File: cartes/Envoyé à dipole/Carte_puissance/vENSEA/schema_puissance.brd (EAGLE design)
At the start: 73.7 x 46.6 mm, 23 parts, among them X2 GMSTBA2

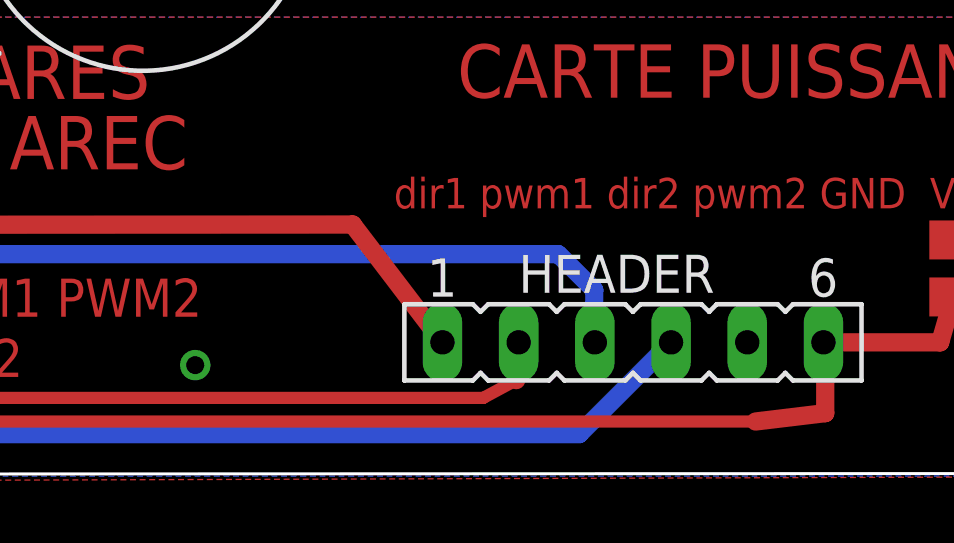
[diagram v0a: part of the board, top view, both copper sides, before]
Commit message: Maj carte puissance vENSEA + correction bug + modif carte RF-CAN
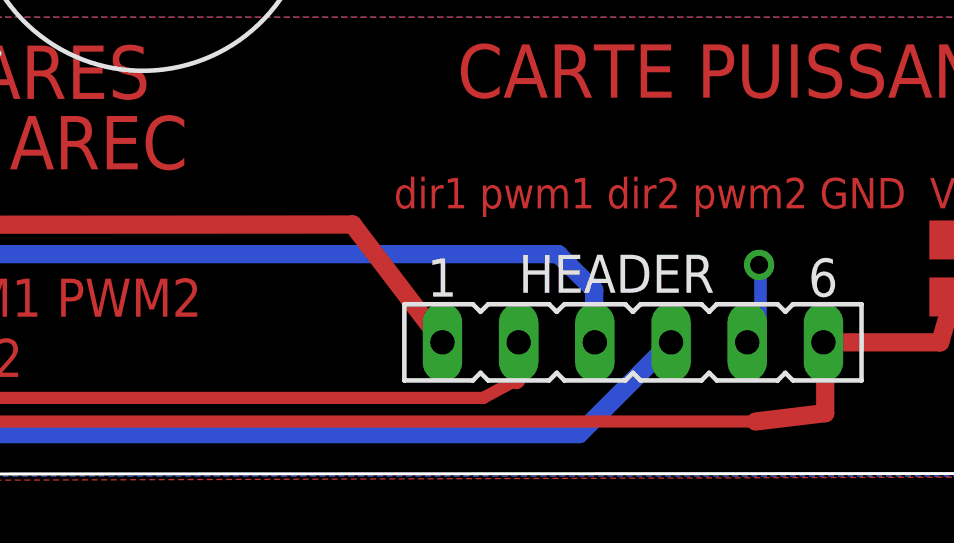
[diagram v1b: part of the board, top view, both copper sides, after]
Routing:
- net GND: track 1.31 -> 4.59 mm
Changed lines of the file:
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@@
 <layers>
 <layer number="1" name="Top" color="4" fill="1" visible="yes" active="yes"/>
-<layer number="16" name="Bottom" color="1" fill="1" visible="no" active="yes"/>
+<layer number="16" name="Bottom" color="1" fill="1" visible="yes" active="yes"/>
 <layer number="17" name="Pads" color="2" fill="1" visible="yes" active="yes"/>
 <layer number="18" name="Vias" color="2" fill="1" visible="yes" active="yes"/>
 <layer number="19" name="Unrouted" color="6" fill="1" visible="yes" active="yes"/>
-<layer number="20" name="Dimension" color="15" fill="1" visible="no" active="yes"/>
-<layer number="21" name="tPlace" color="7" fill="1" visible="no" active="yes"/>
-<layer number="22" name="bPlace" color="7" fill="1" visible="no" active="yes"/>
-<layer number="23" name="tOrigins" color="15" fill="1" visible="no" active="yes"/>
-<layer number="24" name="bOrigins" color="15" fill="1" visible="no" active="yes"/>
-<layer number="25" name="tNames" color="7" fill="1" visible="no" active="yes"/>
-<layer number="26" name="bNames" color="7" fill="1" visible="no" active="yes"/>
-<layer number="27" name="tValues" color="7" fill="1" visible="no" active="yes"/>
-<layer number="28" name="bValues" color="7" fill="1" visible="no" active="yes"/>
-<layer number="29" name="tStop" color="7" fill="3" visible="no" active="yes"/>
-<layer number="30" name="bStop" color="7" fill="6" visible="no" active="yes"/>
-<layer number="31" name="tCream" color="7" fill="4" visible="no" active="yes"/>
-<layer number="32" name="bCream" color="7" fill="5" visible="no" active="yes"/>
-<layer number="33" name="tFinish" color="6" fill="3" visible="no" active="yes"/>
-<layer number="34" name="bFinish" color="6" fill="6" visible="no" active="yes"/>
-<layer number="35" name="tGlue" color="7" fill="4" visible="no" active="yes"/>
-<layer number="36" name="bGlue" color="7" fill="5" visible="no" active="yes"/>
-<layer number="37" name="tTest" color="7" fill="1" visible="no" active="yes"/>
-<layer number="38" name="bTest" color="7" fill="1" visible="no" active="yes"/>
-<layer number="39" name="tKeepout" color="4" fill="11" visible="no" active="yes"/>
-<layer number="40" name="bKeepout" color="1" fill="11" visible="no" active="yes"/>
-<layer number="41" name="tRestrict" color="4" fill="10" visible="no" active="yes"/>
-<layer number="42" name="bRestrict" color="1" fill="10" visible="no" active="yes"/>
-<layer number="43" name="vRestrict" color="2" fill="10" visible="no" active="yes"/>
-<layer number="44" name="Drills" color="7" fill="1" visible="no" active="yes"/>
-<layer number="45" name="Holes" color="7" fill="1" visible="no" active="yes"/>
-<layer number="46" name="Milling" color="3" fill="1" visible="no" active="yes"/>
-<layer number="47" name="Measures" color="7" fill="1" visible="no" active="yes"/>
-<layer number="48" name="Document" color="7" fill="1" visible="no" active="yes"/>
-<layer number="49" name="Reference" color="7" fill="1" visible="no" active="yes"/>
-<layer number="50" name="dxf" color="7" fill="1" visible="no" active="yes"/>
-<layer number="51" name="tDocu" color="7" fill="1" visible="no" active="yes"/>
-<layer number="52" name="bDocu" color="7" fill="1" visible="no" active="yes"/>
+<layer number="20" name="Dimension" color="15" fill="1" visible="yes" active="yes"/>
+<layer number="21" name="tPlace" color="7" fill="1" visible="yes" active="yes"/>
+<layer number="22" name="bPlace" color="7" fill="1" visible="yes" active="yes"/>
+<layer number="23" name="tOrigins" color="15" fill="1" visible="yes" active="yes"/>
+<layer number="24" name="bOrigins" color="15" fill="1" visible="yes" active="yes"/>
+<layer number="25" name="tNames" color="7" fill="1" visible="yes" active="yes"/>
+<layer number="26" name="bNames" color="7" fill="1" visible="yes" active="yes"/>
+<layer number="27" name="tValues" color="7" fill="1" visible="yes" active="yes"/>
+<layer number="28" name="bValues" color="7" fill="1" visible="yes" active="yes"/>
+<layer number="29" name="tStop" color="7" fill="3" visible="yes" active="yes"/>
+<layer number="30" name="bStop" color="7" fill="6" visible="yes" active="yes"/>
+<layer number="31" name="tCream" color="7" fill="4" visible="yes" active="yes"/>
+<layer number="32" name="bCream" color="7" fill="5" visible="yes" active="yes"/>
+<layer number="33" name="tFinish" color="6" fill="3" visible="yes" active="yes"/>
+<layer number="34" name="bFinish" color="6" fill="6" visible="yes" active="yes"/>
+<layer number="35" name="tGlue" color="7" fill="4" visible="yes" active="yes"/>
+<layer number="36" name="bGlue" color="7" fill="5" visible="yes" active="yes"/>
+<layer number="37" name="tTest" color="7" fill="1" visible="yes" active="yes"/>
+<layer number="38" name="bTest" color="7" fill="1" visible="yes" active="yes"/>
+<layer number="39" name="tKeepout" color="4" fill="11" visible="yes" active="yes"/>
+<layer number="40" name="bKeepout" color="1" fill="11" visible="yes" active="yes"/>
+<layer number="41" name="tRestrict" color="4" fill="10" visible="yes" active="yes"/>
+<layer number="42" name="bRestrict" color="1" fill="10" visible="yes" active="yes"/>
+<layer number="43" name="vRestrict" color="2" fill="10" visible="yes" active="yes"/>
+<layer number="44" name="Drills" color="7" fill="1" visible="yes" active="yes"/>
+<layer number="45" name="Holes" color="7" fill="1" visible="yes" active="yes"/>
+<layer number="46" name="Milling" color="3" fill="1" visible="yes" active="yes"/>
+<layer number="47" name="Measures" color="7" fill="1" visible="yes" active="yes"/>
+<layer number="48" name="Document" color="7" fill="1" visible="yes" active="yes"/>
+<layer number="49" name="Reference" color="7" fill="1" visible="yes" active="yes"/>
+<layer number="50" name="dxf" color="7" fill="1" visible="yes" active="yes"/>
+<layer number="51" name="tDocu" color="7" fill="1" visible="yes" active="yes"/>
+<layer number="52" name="bDocu" color="7" fill="1" visible="yes" active="yes"/>
 <layer number="53" name="tGND_GNDA" color="7" fill="9" visible="no" active="no"/>
 <layer number="54" name="bGND_GNDA" color="1" fill="9" visible="no" active="no"/>
-<layer number="56" name="wert" color="7" fill="1" visible="no" active="yes"/>
+<layer number="56" name="wert" color="7" fill="1" visible="yes" active="yes"/>
 <layer number="91" name="Nets" color="2" fill="1" visible="no" active="no"/>
 <layer number="92" name="Busses" color="1" fill="1" visible="no" active="no"/>
@@
 <layer number="98" name="Guide" color="6" fill="1" visible="no" active="no"/>
 <layer number="100" name="Muster" color="7" fill="1" visible="no" active="no"/>
-<layer number="101" name="Patch_Top" color="12" fill="4" visible="no" active="yes"/>
-<layer number="102" name="Vscore" color="7" fill="1" visible="no" active="yes"/>
-<layer number="104" name="Name" color="7" fill="1" visible="no" active="yes"/>
-<layer number="116" name="Patch_BOT" color="9" fill="4" visible="no" active="yes"/>
-<layer number="121" name="_tsilk" color="7" fill="1" visible="no" active="yes"/>
-<layer number="122" name="_bsilk" color="7" fill="1" visible="no" active="yes"/>
-<layer number="151" name="HeatSink" color="7" fill="1" visible="no" active="yes"/>
-<layer number="200" name="200bmp" color="1" fill="10" visible="no" active="yes"/>
+<layer number="101" name="Patch_Top" color="12" fill="4" visible="yes" active="yes"/>
+<layer number="102" name="Vscore" color="7" fill="1" visible="yes" active="yes"/>
+<layer number="104" name="Name" color="7" fill="1" visible="yes" active="yes"/>
+<layer number="116" name="Patch_BOT" color="9" fill="4" visible="yes" active="yes"/>
+<layer number="121" name="_tsilk" color="7" fill="1" visible="yes" active="yes"/>
+<layer number="122" name="_bsilk" color="7" fill="1" visible="yes" active="yes"/>
+<layer number="151" name="HeatSink" color="7" fill="1" visible="yes" active="yes"/>
+<layer number="200" name="200bmp" color="1" fill="10" visible="yes" active="yes"/>
 <layer number="201" name="201bmp" color="2" fill="1" visible="no" active="no"/>
 <layer number="202" name="202bmp" color="3" fill="1" visible="no" active="no"/>
 <layer number="250" name="Descript" color="3" fill="1" visible="no" active="no"/>
 <layer number="251" name="SMDround" color="12" fill="11" visible="no" active="no"/>
-<layer number="254" name="cooling" color="7" fill="1" visible="no" active="yes"/>
+<layer number="254" name="cooling" color="7" fill="1" visible="yes" active="yes"/>
 </layers>
 <board>
@@
 <vertex x="82.5" y="22"/>
 </polygon>
-<via x="46.7" y="10.4" extent="1-16" drill="0.6" diameter="1.016"/>
+<via x="65.495996875" y="13.742640625" extent="1-16" drill="0.6" diameter="1.016"/>
 <via x="79.9412" y="9.328321875" extent="1-16" drill="3" diameter="1.4224"/>
 <via x="11.32671875" y="9.267359375" extent="1-16" drill="3" diameter="1.4224"/>
@@
 <wire x1="21.9" y1="17.425" x2="21.925" y2="17.4" width="0.6096" layer="1"/>
 <contactref element="INPUT" pad="2"/>
+<wire x1="65.1" y1="11.16" x2="65.542159375" y2="11.16" width="0.4064" layer="16"/>
+<wire x1="65.542159375" y1="11.16" x2="65.542159375" y2="13.573759375" width="0.4064" layer="16"/>
+<wire x1="65.542159375" y1="13.73631875" x2="65.5828" y2="13.73631875" width="0.4064" layer="16"/>
+<wire x1="65.5828" y1="13.73631875" x2="65.5828" y2="13.573759375" width="0.4064" layer="16"/>
+<wire x1="65.5828" y1="13.573759375" x2="65.542159375" y2="13.573759375" width="0.4064" layer="16"/>
+<wire x1="65.542159375" y1="13.573759375" x2="65.542159375" y2="13.73631875" width="0.4064" layer="16"/>
+<wire x1="65.542159375" y1="13.73631875" x2="65.542159375" y2="13.756640625" width="0.4064" layer="16"/>
 </signal>
 <signal name="N$2">
